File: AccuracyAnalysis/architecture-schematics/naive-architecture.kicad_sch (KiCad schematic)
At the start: 9 parts, among them Q2 Q_NMOS_GDS

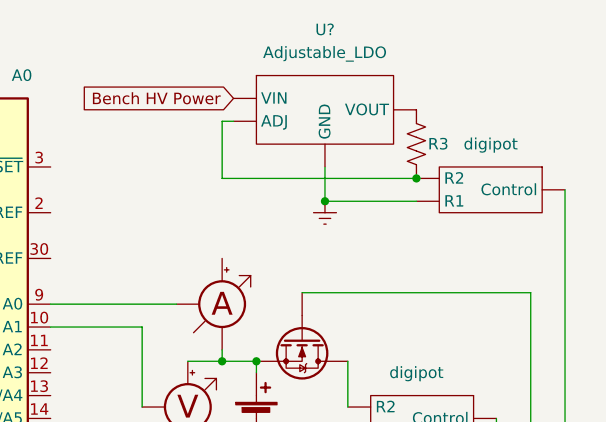
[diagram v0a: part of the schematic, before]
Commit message: fix disconnect in schematic
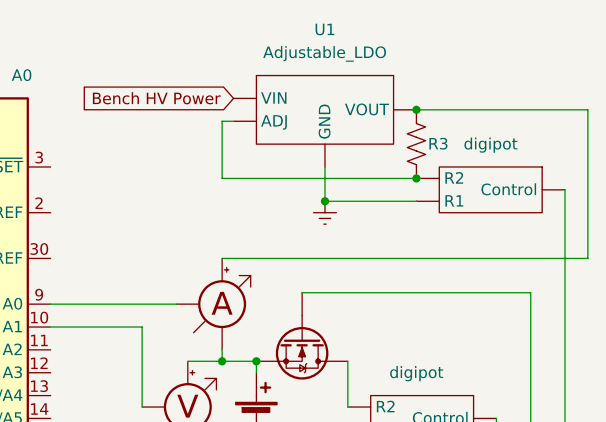
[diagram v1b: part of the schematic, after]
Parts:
- gave numbers to parts that had none: 1
- renumbered R2 to R1
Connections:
- net at R3.1, U1. (VOUT): now also MES2.2 (+)
- new net: R2. (R2), R3.2, U1. (VOUT)
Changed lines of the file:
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@@
   (junction (at 168.91 86.36) (diameter 0) (color 0 0 0 0)
   )
+  (junction (at 179.07 76.2) (diameter 0) (color 0 0 0 0)
+  )
   (junction (at 161.29 104.14) (diameter 0) (color 0 0 0 0)
   )
@@
     (stroke (width 0) (type default) (color 0 0 0 0))
   )
+  (wire (pts (xy 198.12 92.71) (xy 157.48 92.71))
+    (stroke (width 0) (type default) (color 0 0 0 0))
+  )
   (wire (pts (xy 123.19 125.73) (xy 125.73 125.73))
     (stroke (width 0) (type default) (color 0 0 0 0))
@@
     (stroke (width 0) (type default) (color 0 0 0 0))
   )
+  (wire (pts (xy 198.12 76.2) (xy 198.12 92.71))
+    (stroke (width 0) (type default) (color 0 0 0 0))
+  )
   (wire (pts (xy 138.43 97.79) (xy 152.4 97.79))
     (stroke (width 0) (type default) (color 0 0 0 0))
@@
   )
   (wire (pts (xy 179.07 86.36) (xy 168.91 86.36))
+    (stroke (width 0) (type default) (color 0 0 0 0))
+  )
+  (wire (pts (xy 179.07 76.2) (xy 198.12 76.2))
     (stroke (width 0) (type default) (color 0 0 0 0))
   )
@@
   (symbol (lib_id "Rapid-EPS_architecture-blocks:Adjustable_LDO") (at 168.91 67.31 0) (unit 1)
     (in_bom yes) (on_board yes) (fields_autoplaced)
-    (property "Reference" "U?" (id 0) (at 168.91 67.31 0))
+    (property "Reference" "U1" (id 0) (at 168.91 67.31 0))
     (property "Value" "Adjustable_LDO" (id 1) (at 168.91 69.85 0))
     (property "Footprint" "" (id 2) (at 168.91 67.31 0)
@@
   (symbol (lib_name "digipot_1") (lib_id "Rapid-EPS_architecture-blocks:digipot") (at 185.42 107.95 0) (mirror y) (unit 1)
     (in_bom yes) (on_board yes) (fields_autoplaced)
-    (property "Reference" "R2" (id 0) (at 179.07 102.87 0)
-      (effects (font (size 1.27 1.27)) hide)
-    )
+    (property "Reference" "R1" (id 0) (at 179.07 102.87 0)
+      (effects (font (size 1.27 1.27)) hide)
+    )

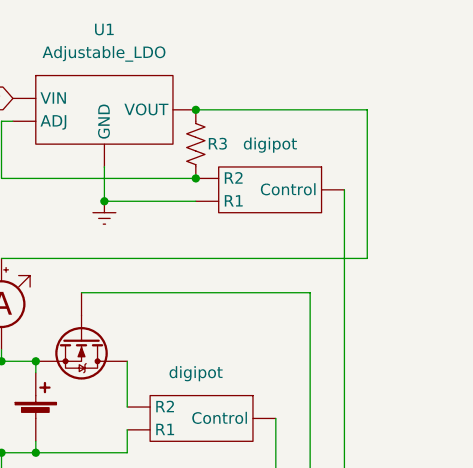
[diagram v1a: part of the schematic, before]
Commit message: write control mode analyses for naive implementation
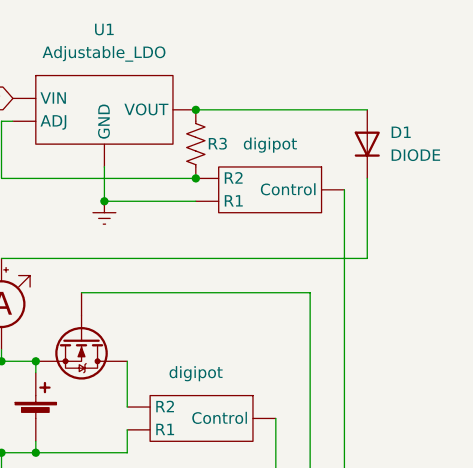
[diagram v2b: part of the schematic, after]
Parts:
- added D1: DIODE, symbol Simulation_SPICE:DIODE
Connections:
- new net: D1.1 (A), R3.1, U1. (VOUT)
- new net: R2. (R2), R3.2, U1. (VOUT)
- new net: D1.2 (K), MES2.2 (+)
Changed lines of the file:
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@@
-    (stroke (width 0) (type default) (color 0 0 0 0))
-  )
-  (wire (pts (xy 198.12 76.2) (xy 198.12 92.71))
     (stroke (width 0) (type default) (color 0 0 0 0))
   )
@@
   )
   (wire (pts (xy 123.19 125.73) (xy 123.19 128.27))
+    (stroke (width 0) (type default) (color 0 0 0 0))
+  )
+  (wire (pts (xy 198.12 83.82) (xy 198.12 92.71))
     (stroke (width 0) (type default) (color 0 0 0 0))
   )
@@
     (pin "")
   )
+  (symbol (lib_id "Simulation_SPICE:DIODE") (at 198.12 80.01 270) (unit 1)
+    (in_bom yes) (on_board yes)
+    (property "Reference" "D1" (id 0) (at 200.66 78.7399 90)
+      (effects (font (size 1.27 1.27)) (justify left))
+    )
+    (property "Value" "DIODE" (id 1) (at 200.66 81.2799 90)
+      (effects (font (size 1.27 1.27)) (justify left))
+    )
+    (property "Footprint" "" (id 2) (at 198.12 80.01 0)
+      (effects (font (size 1.27 1.27)) hide)
+    )
+    (property "Datasheet" "~" (id 3) (at 198.12 80.01 0)
+      (effects (font (size 1.27 1.27)) hide)
+    )
+    (property "Spice_Netlist_Enabled" "Y" (id 4) (at 198.12 80.01 0)
+      (effects (font (size 1.27 1.27)) (justify left) hide)
+    )
+    (property "Spice_Primitive" "D" (id 5) (at 198.12 80.01 0)
+      (effects (font (size 1.27 1.27)) (justify left) hide)
+    )
+    (pin "1")
+    (pin "2")
+  )
   (symbol (lib_id "Rapid-EPS_architecture-blocks:Ammeter_DIO") (at 157.48 97.79 0) (unit 1)
